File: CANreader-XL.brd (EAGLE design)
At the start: 99.8 x 49.8 mm, 99 parts, among them IC1 STM32F107RBT, IC2 TJA1055T/3, IC3 BD9G101G, IC4 LM1117IMPX-3.3, IC5 MCP2562-SOIC8, IC7 DP83848I, Q1 25MHz, SW1 SLEEP, SW2 TERM, U1 HC_05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

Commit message: BOOT selection
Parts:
- removed R9: 10K, rcl:R0805
- added JP1: BOOT, pinhead:1X03
- added R6: 10K, rcl:R0805
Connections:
- new net N$29: JP1.2, R6.1
- net +3V3: now also JP1.3
- net GND: now also JP1.1; no longer R9.1
- net N$3: now also R6.2; no longer R9.2
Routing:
- net N$3: track 10.5 -> 0.00 mm, vias 1 -> 0
- net GND: track 854.0 -> 853.3 mm
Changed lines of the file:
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@@
 <attribute name="VALUE" x="53.34" y="4.826" size="1.27" layer="28" rot="MR270"/>
-</element>
-<element name="R9" library="rcl" package="R0805" value="10K" x="48.006" y="25.908" smashed="yes" rot="MR270">
-<attribute name="NAME" x="47.248" y="23.618" size="0.8128" layer="26" rot="MR180" align="center-left"/>
-<attribute name="VALUE" x="50.546" y="26.543" size="1.27" layer="28" rot="MR270"/>
 </element>
 <element name="R10" library="rcl" package="R0805" value="10K" x="66.802" y="16.891" smashed="yes" rot="MR270">
@@
 <element name="IC5" library="STM32_CAN-USB" package="SOIC8-1.27-5X4MM" value="MCP2562-SOIC8" x="16.002" y="14.732" rot="R90"/>
 <element name="C40" library="rcl" package="C0805" value="0.1uF" x="-9.144" y="-16.002"/>
+<element name="JP1" library="pinhead" package="1X03" value="BOOT" x="-6.858" y="-22.606"/>
+<element name="R6" library="rcl" package="R0805" value="10K" x="-9.144" y="-27.686"/>
 </elements>
 <signals>
@@
 <contactref element="C1" pad="2"/>
 <contactref element="C3" pad="1"/>
-<contactref element="R9" pad="1"/>
 <contactref element="U1" pad="21"/>
 <contactref element="U1" pad="13"/>
@@
 <wire x1="50.546" y1="2.199" x2="50.546" y2="0.762" width="0.8128" layer="1"/>
 <wire x1="46.99" y1="1.895" x2="46.99" y2="0.762" width="0.8128" layer="1"/>
-<wire x1="48.006" y1="26.858" x2="47.31" y2="26.858" width="0.3048" layer="16"/>
 <via x="44.45" y="27.686" extent="1-16" drill="0.6"/>
 <wire x1="43.688" y1="27.686" x2="44.45" y2="27.686" width="0.8128" layer="1"/>
@@
 <wire x1="80.01" y1="29.845" x2="83.566" y2="33.401" width="0.3048" layer="16"/>
 <wire x1="83.566" y1="33.401" x2="85.979" y2="33.401" width="0.3048" layer="16"/>
-<wire x1="99.314" y1="49.022" x2="101.6" y2="54.798" width="0" layer="19" extent="1-16"/>
+<contactref element="JP1" pad="1"/>
+<wire x1="99.314" y1="49.022" x2="101.6" y2="54.798" width="0" layer="19" extent="1-1"/>
+<wire x1="51.496" y1="36.576" x2="51.496" y2="36.576" width="0" layer="19" extent="1-16"/>
 <wire x1="99.314" y1="49.022" x2="99.314" y2="49.022" width="0" layer="19" extent="1-16"/>
+<wire x1="51.308" y1="32.766" x2="51.496" y2="33.02" width="0" layer="19" extent="1-16"/>
 <wire x1="14.478" y1="16.317" x2="14.986" y2="16.637" width="0" layer="19" extent="1-16"/>
 <wire x1="18.702" y1="14.097" x2="17.399" y2="14.097" width="0" layer="19" extent="1-1"/>
-<wire x1="101.6" y1="48.194" x2="99.314" y2="49.022" width="0" layer="19" extent="1-16"/>
+<wire x1="49.582" y1="39.318" x2="48.26" y2="39.37" width="0" layer="19" extent="1-1"/>
+<wire x1="55.118" y1="34.798" x2="54.61" y2="36.576" width="0" layer="19" extent="1-1"/>
+<wire x1="50.546" y1="34.798" x2="51.308" y2="36.576" width="0" layer="19" extent="16-16"/>
+<wire x1="52.832" y1="31.242" x2="54.582" y2="30.198" width="0" layer="19" extent="1-1"/>
+<wire x1="52.832" y1="38.354" x2="51.496" y2="36.576" width="0" layer="19" extent="1-1"/>
+<wire x1="101.6" y1="48.194" x2="99.314" y2="49.022" width="0" layer="19" extent="1-1"/>
 <wire x1="60.137" y1="8.001" x2="62.517" y2="5.776" width="0" layer="19" extent="1-16"/>
 <wire x1="68.707" y1="11.22321875" x2="68.937" y2="11.025" width="0" layer="19" extent="16-16"/>
@@
 <wire x1="101.6" y1="42.606" x2="101.6" y2="48.194" width="0" layer="19" extent="1-1"/>
 <wire x1="81.366" y1="39.398" x2="83.566" y2="33.401" width="0" layer="19" extent="1-16"/>
+<wire x1="79.248" y1="38.608" x2="78.966" y2="39.398" width="0" layer="19" extent="1-16"/>
+<wire x1="77.216" y1="40.198" x2="77.216" y2="41.148" width="0" layer="19" extent="1-16"/>
 <wire x1="6.812" y1="30.202" x2="1.399" y2="33.653" width="0" layer="19" extent="1-1"/>
 <wire x1="94.996" y1="54.798" x2="101.6" y2="54.798" width="0" layer="19" extent="1-1"/>
@@
 <wire x1="3.558" y1="13.184" x2="3.558" y2="4.184" width="0" layer="19" extent="1-1"/>
 <wire x1="-10.094" y1="-16.002" x2="0.762" y2="0.762" width="0" layer="19" extent="1-16"/>
+<wire x1="-9.398" y1="-22.606" x2="-10.094" y2="-16.002" width="0" layer="19" extent="1-1"/>
 </signal>
 <signal name="+3V3">
@@
 <wire x1="93.853" y1="32.004" x2="94.742" y2="32.004" width="0.3048" layer="16"/>
 <wire x1="94.742" y1="32.004" x2="96.012" y2="30.734" width="0.3048" layer="16"/>
+<contactref element="JP1" pad="3"/>
 <wire x1="97.602" y1="56.896" x2="101.346" y2="59.878" width="0" layer="19" extent="1-1"/>
 <wire x1="96.012" y1="58.608" x2="97.602" y2="56.896" width="0" layer="19" extent="1-1"/>
@@
 <wire x1="69.86" y1="43.312" x2="72.832" y2="38.398" width="0" layer="19" extent="1-1"/>
 <wire x1="58.582" y1="38.548" x2="69.86" y2="43.312" width="0" layer="19" extent="1-1"/>
-<wire x1="31.75" y1="34.991" x2="31.75" y2="35.052" width="0" layer="19" extent="16-16"/>
+<wire x1="57.205" y1="24.837" x2="55.082" y2="29.048" width="0" layer="19" extent="1-1"/>
+<wire x1="31.75" y1="35.052" x2="31.75" y2="34.991" width="0" layer="19" extent="16-16"/>
 <wire x1="6.558" y1="13.184" x2="4.699" y2="11.684" width="0" layer="19" extent="16-16"/>
 <wire x1="3.812" y1="27.202" x2="3.683" y2="20.193" width="0" layer="19" extent="16-16"/>
@@
 <wire x1="94.742" y1="32.004" x2="101.6" y2="46.294" width="0" layer="19" extent="1-16"/>
 <wire x1="-8.194" y1="-16.002" x2="4.699" y2="11.684" width="0" layer="19" extent="1-16"/>
+<wire x1="-4.318" y1="-22.606" x2="-8.194" y2="-16.002" width="0" layer="19" extent="1-1"/>
 </signal>
 <signal name="CAN1_RX">
@@
 <wire x1="6.812" y1="27.202" x2="47.082" y2="37.548" width="0" layer="19" extent="1-1"/>
 </signal>
-<signal name="N$3">
-<contactref element="R9" pad="2"/>
-<wire x1="48.006" y1="24.958" x2="45.654" y2="24.958" width="0.3048" layer="16"/>
-<wire x1="43.609" y1="31.925" x2="43.18" y2="31.496" width="0.3048" layer="1"/>
-<wire x1="43.18" y1="31.496" x2="43.18" y2="30.988" width="0.3048" layer="1"/>
-<via x="43.18" y="30.988" extent="1-16" drill="0.6"/>
-<wire x1="43.18" y1="30.988" x2="43.18" y2="27.432" width="0.3048" layer="16"/>
-<wire x1="43.18" y1="27.432" x2="45.654" y2="24.958" width="0.3048" layer="16"/>
-<contactref element="IC1" pad="60"/>
-<wire x1="43.609" y1="31.925" x2="47.082" y2="33.048" width="0" layer="19" extent="1-1"/>
-</signal>
 <signal name="N$25">
 <contactref element="U1" pad="34"/>
@@
 <wire x1="18.24" y1="46.909" x2="96.139" y2="44.704" width="0" layer="19" extent="1-1"/>
 </signal>
+<signal name="N$3">
+<contactref element="IC1" pad="60"/>
+<contactref element="R6" pad="2"/>
+<wire x1="-8.194" y1="-27.686" x2="47.082" y2="33.048" width="0" layer="19" extent="1-1"/>
+</signal>
+<signal name="N$29">
+<contactref element="R6" pad="1"/>
+<contactref element="JP1" pad="2"/>
+<wire x1="-6.858" y1="-22.606" x2="-10.094" y2="-27.686" width="0" layer="19" extent="1-1"/>
+</signal>
 </signals>

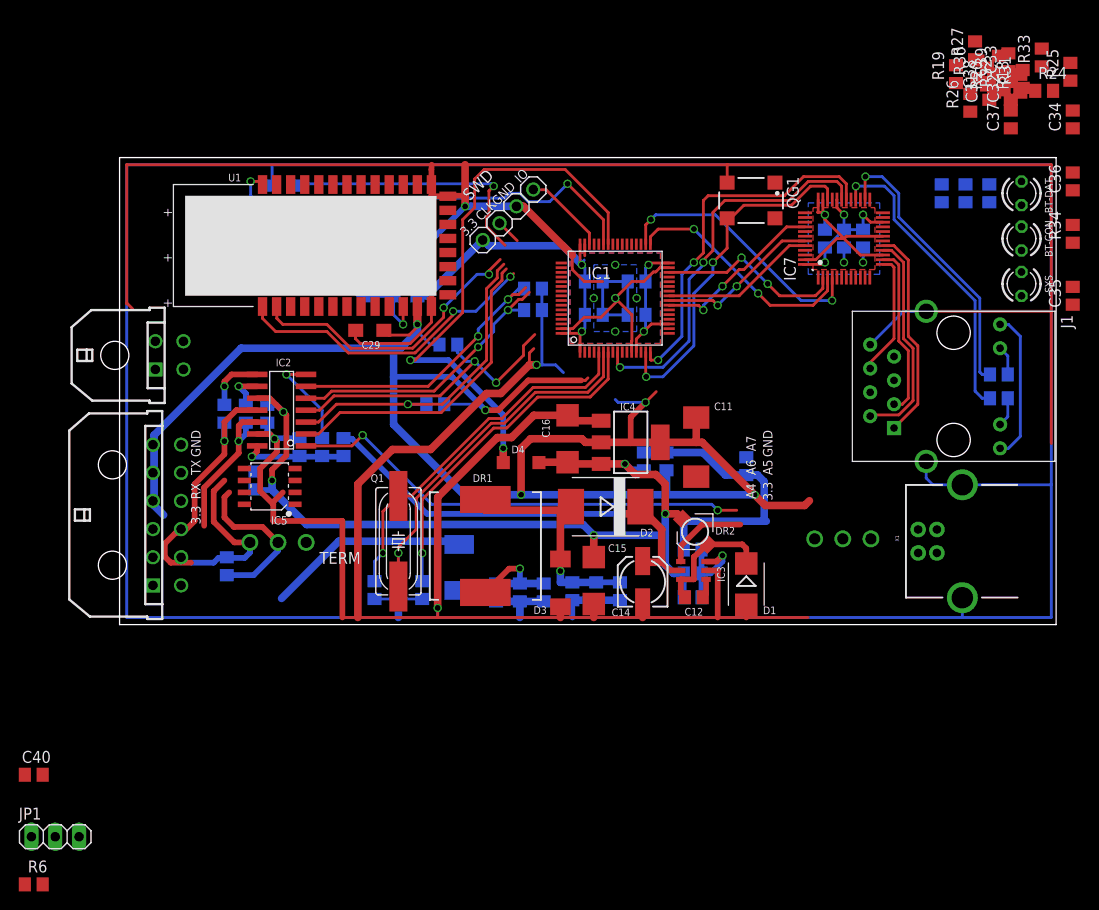
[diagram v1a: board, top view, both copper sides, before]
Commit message: Swap UART, CAN for better routing
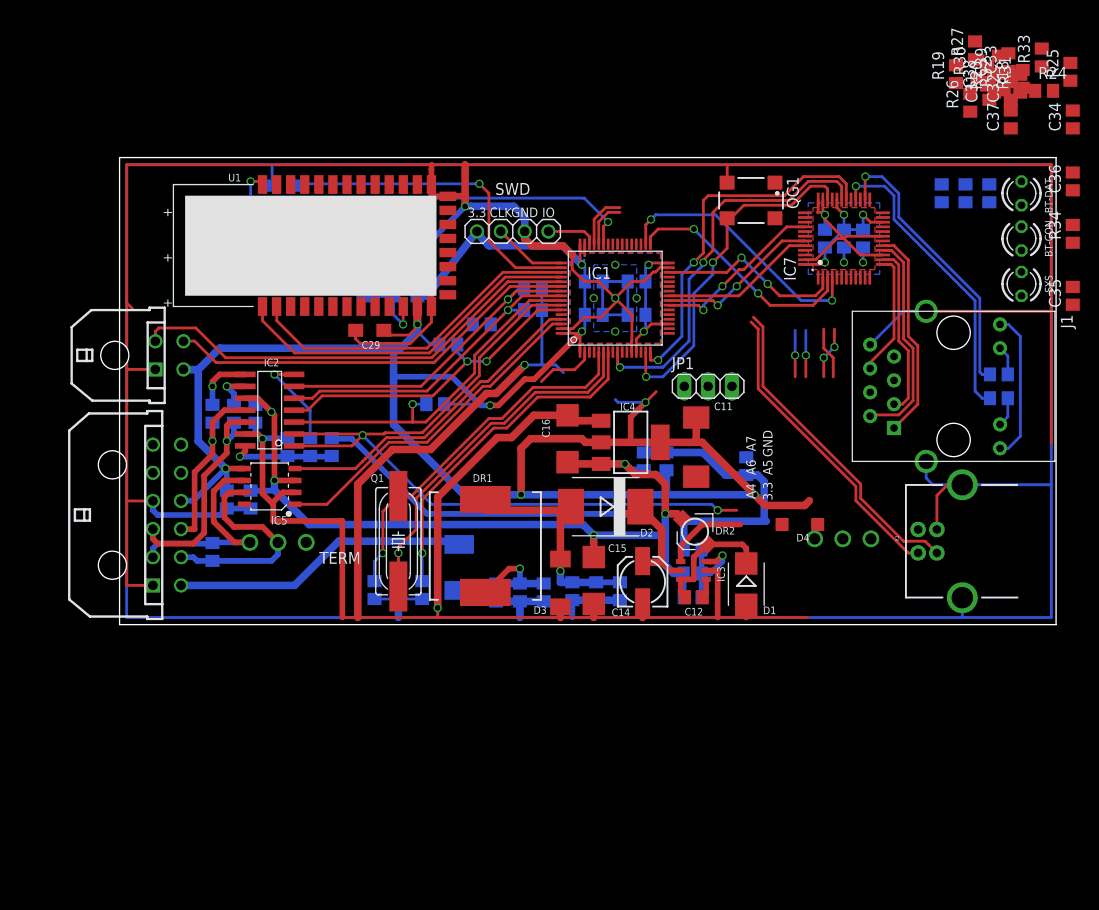
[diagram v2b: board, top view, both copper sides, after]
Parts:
- moved JP1 84.5 mm to (62.7, 25.4)
- moved R6 76.4 mm to (38.6, 32.0), flipped to the bottom
- moved C40 35.8 mm to (11.4, 13.3), flipped to the bottom, turned to 90 degrees
- moved D4 30.4 mm to (72.5, 10.7), turned to 0 degrees
- moved R22 2.16 mm to (9.91, 7.75)
- moved C26 2.09 mm to (14.0, 13.3), turned to 90 degrees
- moved X2 1.85 mm to (41.9, 41.9), turned to 0 degrees
- moved C10 1.27 mm to (17.9, 18.9)
- moved C9 1.27 mm to (14.5, 22.5)
- moved IC2 1.27 mm to (16.0, 22.9)
- moved R1 1.27 mm to (12.2, 22.5)
- moved R2 1.27 mm to (9.91, 22.5)
- moved R3 1.27 mm to (20.3, 18.9)
- moved R4 1.27 mm to (22.6, 18.9)
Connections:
- net +3V3: now also X4.P$3; no longer X4.P$1
- net CAN1_RX: now also IC5.4; no longer IC2.3, R5.1
- net CAN1_TX: now also IC5.1; no longer IC2.2
- net CAN2_RX: now also IC2.3, R5.1; no longer IC5.4
- net CAN2_TX: now also IC2.2; no longer IC5.1
- net GND: now also X4.P$1; no longer X4.P$4
- net UART4_RX: now also U1.1; no longer X4.P$2
- net UART4_TX: now also U1.2; no longer X4.P$3
- net UART5_RX: now also X4.P$4; no longer U1.1
- net UART5_TX: now also X4.P$2; no longer U1.2
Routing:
- net USB_VBUS: track 59.8 -> 0.00 mm, vias 2 -> 0
- net GND: track 853.3 -> 912.5 mm
- net USB_D+: track 0.00 -> 40.5 mm
- net CAN2_RX: track 0.00 -> 38.3 mm, vias 0 -> 1
- net UART4_RX: track 0.00 -> 38.1 mm
- net USB_D-: track 0.00 -> 37.7 mm
- net UART4_TX: track 0.00 -> 36.4 mm
- net CAN2_TX: track 0.00 -> 35.3 mm
- net UART5_TX: track 31.2 -> 49.1 mm, vias 2 -> 0
- net UART5_RX: track 33.3 -> 44.6 mm, vias 2 -> 0
- net +12V: track 21.6 -> 31.7 mm
- net +3V3: track 274.9 -> 284.6 mm, vias 12 -> 13
- net CAN1L: track 16.6 -> 24.0 mm
- net CAN1H: track 26.5 -> 19.7 mm
- net CAN2_STBY: track 0.00 -> 6.39 mm
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
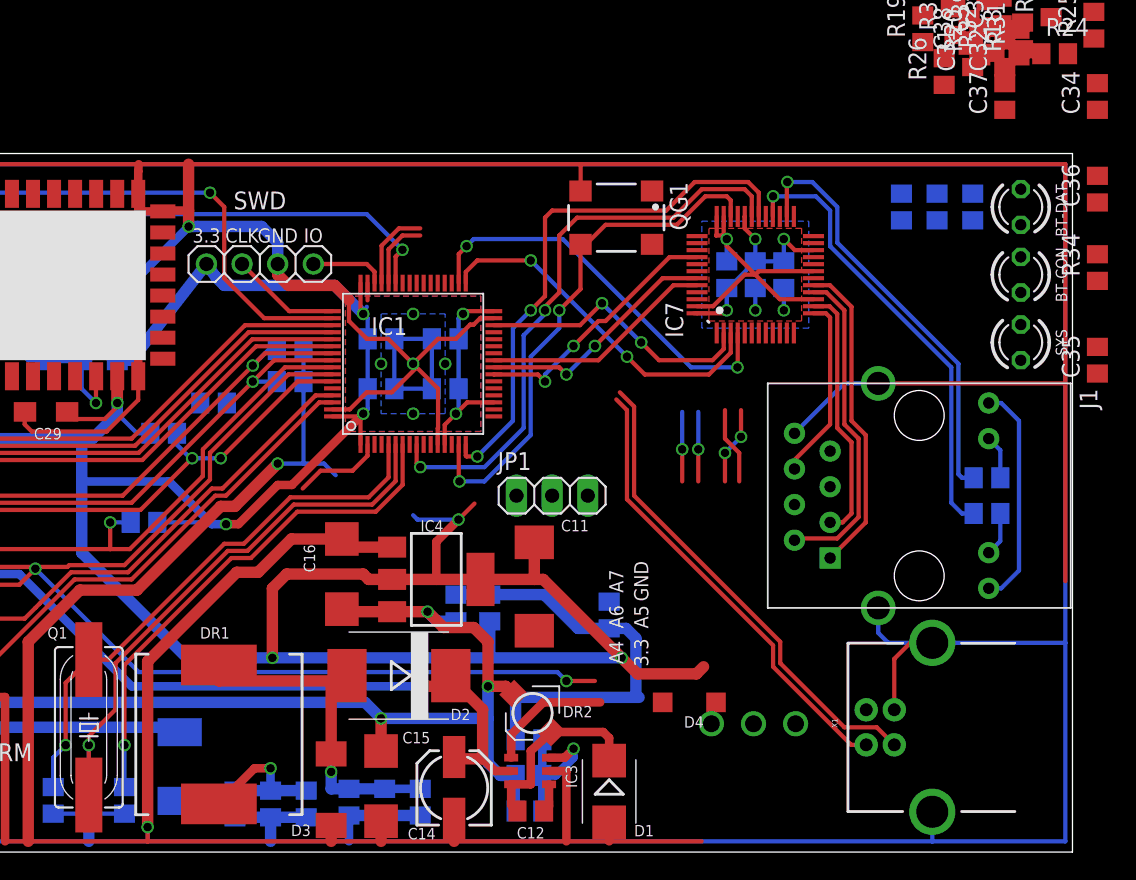
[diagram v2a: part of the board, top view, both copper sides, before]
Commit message: Swap ports
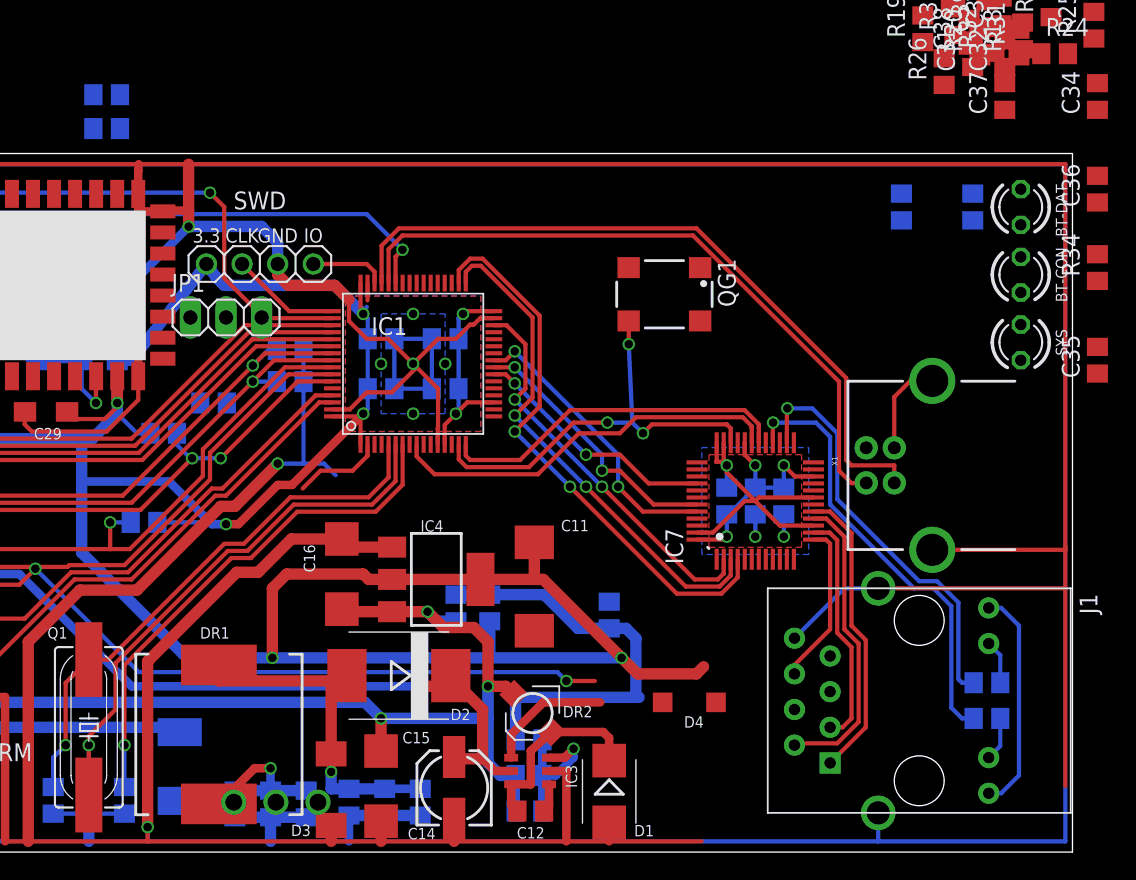
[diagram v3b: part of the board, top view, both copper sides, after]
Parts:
- added R9: 470, rcl:R0805
- moved R14 59.7 mm to (31.0, 54.0), turned to 180 degrees
- moved SW1 34.5 mm to (43.1, 3.56)
- moved JP1 26.5 mm to (39.5, 38.1)
- moved X1 18.7 mm to (87.1, 27.6)
- moved C28 16.1 mm to (77.2, 25.0)
- moved C30 16.1 mm to (79.2, 25.0)
- moved C8 16.1 mm to (75.2, 25.0)
- moved IC7 16.1 mm to (77.2, 25.0)
- moved R28 14.6 mm to (93.7, 12.1)
- moved J1 14.6 mm to (88.9, 10.8)
- moved R29 14.6 mm to (93.7, 9.53)
- moved QG1 6.45 mm to (70.7, 39.8)
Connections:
- new net N$33: LED3.A, R14.2, R9.2
- net GND: now also LED2.K, LED3.K; no longer R13.1, R14.1
- net N$10: now also R13.2; no longer LED2.A
- net N$11: now also LED2.A, R13.1; no longer LED2.K, R13.2
- net N$13: now also R9.1, U1.24; no longer LED3.K, R14.2
- net N$5: now also R14.1; no longer LED3.A
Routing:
- net RMII_MDIO: track 39.0 -> 25.0 mm, vias 2 -> 0
- net RMII_MDC: track 41.7 -> 28.4 mm, vias 2 -> 0
- net RMII_TXD1: track 28.6 -> 40.2 mm
- net RMII_TXD0: track 25.4 -> 36.7 mm
- net USB_D+: track 40.5 -> 51.4 mm
- net USB_D-: track 37.7 -> 47.9 mm
- net +3V3: track 284.6 -> 274.5 mm, vias 13 -> 12
- net RMII_TX_EN: track 20.2 -> 28.5 mm
- net GND: track 912.5 -> 919.2 mm
- net RMII_REF_CLK: track 37.5 -> 31.0 mm, vias 2 -> 3
- net N$32: track 5.55 -> 0.00 mm, vias 2 -> 0
- net N$31: track 5.50 -> 0.00 mm
- net N$24: track 4.95 -> 0.00 mm, vias 1 -> 0
- net N$15: track 4.95 -> 0.00 mm, vias 1 -> 0
- net RMII_RXD1: track 16.7 -> 20.8 mm, vias 0 -> 2
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
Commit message: Attrmpt to route
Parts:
- moved R25 57.7 mm to (74.0, 8.13), flipped to the bottom, turned to 0 degrees
- moved R24 56.7 mm to (74.0, 5.71), flipped to the bottom, turned to 180 degrees
- moved C36 52.0 mm to (74.0, 3.17), flipped to the bottom, turned to 0 degrees
- moved C38 49.2 mm to (86.6, 9.53), flipped to the bottom, turned to 180 degrees
- moved R27 48.5 mm to (74.0, 15.9), flipped to the bottom, turned to 0 degrees
- moved C39 48.2 mm to (86.6, 12.1), flipped to the bottom, turned to 180 degrees
- moved C37 48.0 mm to (74.0, 10.7), flipped to the bottom, turned to 0 degrees
- moved R26 45.6 mm to (74.0, 13.2), flipped to the bottom, turned to 180 degrees
- moved C33 38.2 mm to (81.4, 24.1), flipped to the bottom, turned to 180 degrees
- moved R30 37.8 mm to (85.5, 21.8), flipped to the bottom, turned to 180 degrees
- moved R31 35.7 mm to (85.5, 24.1), flipped to the bottom, turned to 180 degrees
- moved R20 34.8 mm to (67.3, 34.4), flipped to the bottom, turned to 270 degrees
- moved R19 34.2 mm to (65.0, 34.4), flipped to the bottom, turned to 270 degrees
- moved C32 33.9 mm to (69.6, 34.4), flipped to the bottom
- moved R18 32.6 mm to (73.7, 33.9), flipped to the bottom
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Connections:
- removed net N$30: J1.P5
- net +3V3: now also J1.P4, J1.P5
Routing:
- net N$33: track 0.00 -> 75.7 mm
- net N$10: track 0.00 -> 74.6 mm, vias 0 -> 1
- net +3V3: track 274.5 -> 346.0 mm
- net GND: track 919.2 -> 973.4 mm
- net N$6: track 0.00 -> 35.6 mm
- net PFB: track 0.00 -> 30.3 mm, vias 0 -> 3
- net RD+: track 16.8 -> 28.0 mm
- net N$13: track 0.00 -> 10.5 mm, vias 0 -> 1
- net N$21: track 0.00 -> 10.4 mm, vias 0 -> 1
- net N$17: track 0.00 -> 10.0 mm, vias 0 -> 1
- net N$14: track 0.00 -> 9.95 mm
- net TD+: track 21.2 -> 30.8 mm
- net N$11: track 0.00 -> 9.00 mm
- net N$20: track 0.00 -> 8.72 mm, vias 0 -> 1
- net LEDACT_LINK: track 29.8 -> 37.5 mm
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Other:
- board text removed: "A4"
- board text removed: "A5"
- board text removed: "A6"
- board text removed: "A7"

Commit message: Route attempt
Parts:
- moved C11 37.7 mm to (90.8, 42.5)
- moved C16 37.7 mm to (77.1, 43.4)
- moved C17 37.7 mm to (85.2, 41.0)
- moved C18 37.7 mm to (87.6, 41.0)
- moved IC4 37.7 mm to (83.8, 43.1)
- moved C2 30.3 mm to (52.6, 23.5)
- moved C1 30.3 mm to (50.0, 23.5)
- moved C3 30.3 mm to (55.1, 23.5)
- moved Q1 26.1 mm to (51.3, 23.5), turned to 180 degrees
- moved JP1 19.1 mm to (40.3, 19.1), turned to 180 degrees
- moved SW1 13.8 mm to (30.2, 8.64)
- moved X2 8.05 mm to (34.0, 40.3), turned to 90 degrees
- moved C27 4.95 mm to (21.7, 35.9)
- moved C29 4.95 mm to (21.7, 31.4)
- moved R9 4.95 mm to (18.9, 45.8)
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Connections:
- net HC_KEY: now also IC1.41; no longer IC1.50
- net N$6: now also IC1.35; no longer IC1.41
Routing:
- net +3V3: track 346.0 -> 309.7 mm, vias 12 -> 10
- net USB_VBUS: track 6.15 -> 38.8 mm
- net NRST: track 36.7 -> 5.86 mm
- net GND: track 973.4 -> 942.6 mm, vias 12 -> 11
- net N$2: track 41.1 -> 10.5 mm
- net N$1: track 39.2 -> 10.5 mm
- net SWDIO: track 5.40 -> 18.0 mm
- net HC_KEY: track 36.9 -> 49.0 mm
- net +5V: track 94.0 -> 85.6 mm
- net N$15: track 0.00 -> 6.50 mm
- net SWCLK: track 7.83 -> 13.2 mm
- net N$10: track 74.6 -> 79.8 mm
- net UART4_TX: track 36.4 -> 41.5 mm
- net N$33: track 75.7 -> 80.8 mm
- net CAN2H: track 23.4 -> 18.4 mm
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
